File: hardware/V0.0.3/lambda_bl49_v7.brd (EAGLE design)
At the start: 25 x 60 mm, 58 parts, among them IC10 MCP2551-E/SN, IC3 LMV321IDBVR, IC4 TLS115B0EJXUMA1, IC6 TLE4270-2D, IC9 CJ125_32, Q3 ABM3-16.000MHZ-D2Y-T

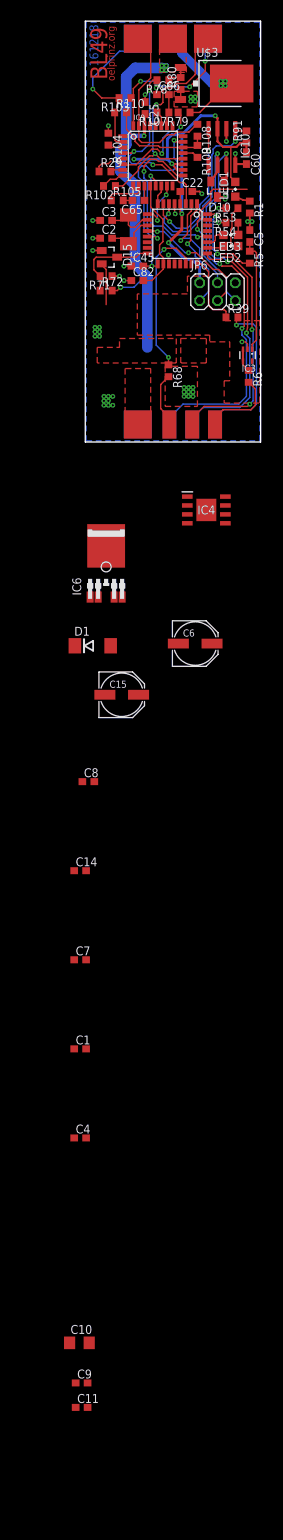
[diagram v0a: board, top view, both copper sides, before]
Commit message: tls115 replaced by ti ref5050
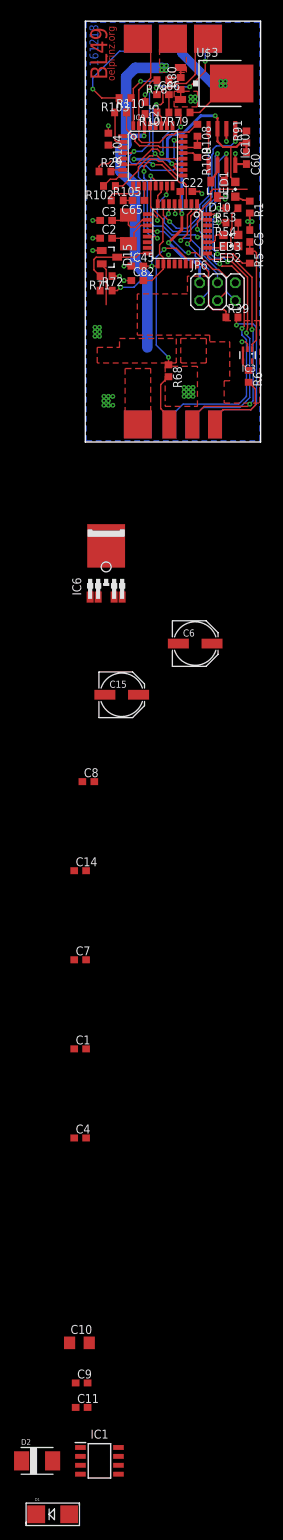
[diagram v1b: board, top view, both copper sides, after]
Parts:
- removed IC4: TLS115B0EJXUMA1, Heinrich:SOIC127P600X170-9N
- added D2: P6SMB18A, Heinrich:DO-214AA
- added IC1: REF50XX, Heinrich:SOIC127P600X175-8N
- D1: value SMBJ36CA -> S1J; device Heinrich:DO214AA -> Heinrich:SMADIODE
- moved D1 124.0 mm to (-4.76, -153.0)
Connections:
- new net VBAT: C1.1, C14.1, C15.+, C6.+, D1.C, D2.P$1, IC1.2, IC6.1
- net +5V: no longer IC4.5
- net +UB: now also D1.A; no longer C1.1, C14.1, C15.+, C6.+, D1.C, IC4.7, IC4.8, IC6.1
- net AREF: now also IC1.6; no longer IC4.1
- net GND: now also D2.P$2, IC1.4; no longer D1.A, IC4.3, IC4.9
